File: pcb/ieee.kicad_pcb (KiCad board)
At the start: 2 copper layers, 152.4 x 114.3 mm, 45 parts, among them J1 Conn_01x20_Pin, J2 Conn_01x20_Pin, J3 Screw_Terminal_01x02, J4 I2C_LCD, J5 Conn_01x20_Pin, J6 Conn_01x20_Pin, M1 FL, M2 FR, M3 RL, M4 RR, M5 Corkscrew, M6 Crank, M7 Fingers, SW1 SW_SPST, U1 TB9051FTG, U10 TCS34725, U11 TCS34725, U12 TB9051FTG, U13 TB9051FTG, U14 IR_Transmitter, U2 TB9051FTG, U3 TB9051FTG, U4 TB9051FTG, U5 PCA9543AD_118, U6 SN74LVC8T245NSR, U7 DRV8833, U8 DRV8833, U9 D36V50F5

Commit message: Fix ERC issues and layout connectors
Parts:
- added R2: 100K, Resistor_THT:R_Axial_DIN0309_L9.0mm_D3.2mm_P15.24mm_Horizontal, F.Cu at (101.9, 119.7)
- added R4: 100K, Resistor_THT:R_Axial_DIN0309_L9.0mm_D3.2mm_P15.24mm_Horizontal, F.Cu at (101.9, 124.5)
- moved M6 314.1 mm to (160.3, 144.8), turned to -90 degrees
- moved U2 305.5 mm to (99.1, 110.7)
- moved J4 303.7 mm to (112.8, 113.8), turned to 180 degrees
- moved A2 302.5 mm to (114.0, 136.9), turned to -90 degrees
- moved U4 260.5 mm to (85.1, 116.1)
- moved S1 256.8 mm to (84.1, 144.8), turned to 90 degrees
- moved U13 250.4 mm to (153.9, 128.5), turned to -90 degrees
- moved JP1 250.4 mm to (199.9, 63.2)
- moved JP2 250.4 mm to (199.4, 58.2)
- moved JP3 250.4 mm to (178.5, 58.7)
- moved JP4 250.4 mm to (178.5, 62.3)
- moved U12 249.9 mm to (144.5, 66.0), turned to 0 degrees
- moved M7 249.5 mm to (147.1, 112.3), turned to 90 degrees
- moved U14 245.7 mm to (153.4, 96.0)
- moved R1 244.6 mm to (158.8, 42.9), turned to -90 degrees
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- renumbered A3 to A2, A2 to A3, J3 to J1, J1 to J2, J2 to J3, M3 to M2, M2 to M3, M7 to M5, M5 to M6, M6 to M7, R2 to R1, R1 to R3, U11 to U1, U4 to U10, U7 to U11, U8 to U12, U12 to U13, U13 to U14, U5 to U2, U9 to U3, U10 to U4, U14 to U5, U1 to U7, U3 to U8, U2 to U9
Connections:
- A1 pad 10: /pico_subsystem/RPI_RX -> /RPI_RX
- A1 pad 8: /pico_subsystem/RPI_TX -> /RPI_TX
- A3 pad 1: /pico_subsystem/RPI_RX -> /RPI_RX
- A3 pad 2: /pico_subsystem/RPI_TX -> /RPI_TX
- J2 pad 2: /SDA -> /RPI_SDA
- J2 pad 3: /SCL -> /RPI_SCL
- J5 pad 1: /pico_subsystem/RPI_RX -> /RPI_RX
- J5 pad 2: /pico_subsystem/RPI_TX -> /RPI_TX
- J6 pad 13: GND -> /pico_subsystem/PICO_AGND
- U12 pad 11: unconnected-(U8-IN3-Pad11) -> /RPI_GPIO10
- U12 pad 12: unconnected-(U8-IN4-Pad12) -> /RPI_GPIO11
- U12 pad 7: unconnected-(U8-IN1-Pad7) -> /RPI_GPIO8
- U12 pad 8: unconnected-(U8-IN2-Pad8) -> /RPI_GPIO9
- U13 pad 7: unconnected-(U12-PWM2-Pad7) -> /RPI_GPIO17
- U13 pad 8: unconnected-(U12-PWM1-Pad8) -> /RPI_GPIO16
- U14 pad 7: unconnected-(U13-PWM2-Pad7) -> /manipulation/CRANK_PWM2
- U14 pad 8: unconnected-(U13-PWM1-Pad8) -> /manipulation/CRANK_PWM1
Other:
- copper layers 2 -> 4

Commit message: Start routing
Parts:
- moved U6 33.2 mm to (175.3, 120.4), turned to 180 degrees
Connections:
- J6 pad 13: /pico_subsystem/PICO_AGND -> GND
- J6 pad 8: GND -> /pico_subsystem/PICO_AGND
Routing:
- net /pico_subsystem/FR_ENCB_5V: track 0.00 -> 139.0 mm
- net /pico_subsystem/FR_ENCA_5V: track 0.00 -> 137.3 mm
- net /pico_subsystem/RR_ENCA_5V: track 0.00 -> 132.4 mm
- net /pico_subsystem/RR_ENCB_5V: track 0.00 -> 130.5 mm
- net /pico_subsystem/FL_ENCB_5V: track 0.00 -> 121.6 mm
- net /pico_subsystem/FL_ENCA_5V: track 0.00 -> 121.1 mm
- net GND: track 0.00 -> 110.7 mm
- net /RPI_PWM3: track 0.00 -> 46.4 mm
- net ENABLE: track 0.00 -> 44.1 mm
- net /pico_subsystem/PICO_3V3: track 0.00 -> 43.1 mm
- net /pico_subsystem/FL_ENCA: track 0.00 -> 37.0 mm
- net /RPI_PWM2: track 0.00 -> 35.6 mm
- net /RPI_GPIO26: track 0.00 -> 31.6 mm
- net /pico_subsystem/FL_ENCB: track 0.00 -> 31.4 mm
- net /pico_subsystem/FR_ENCA: track 0.00 -> 28.3 mm
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
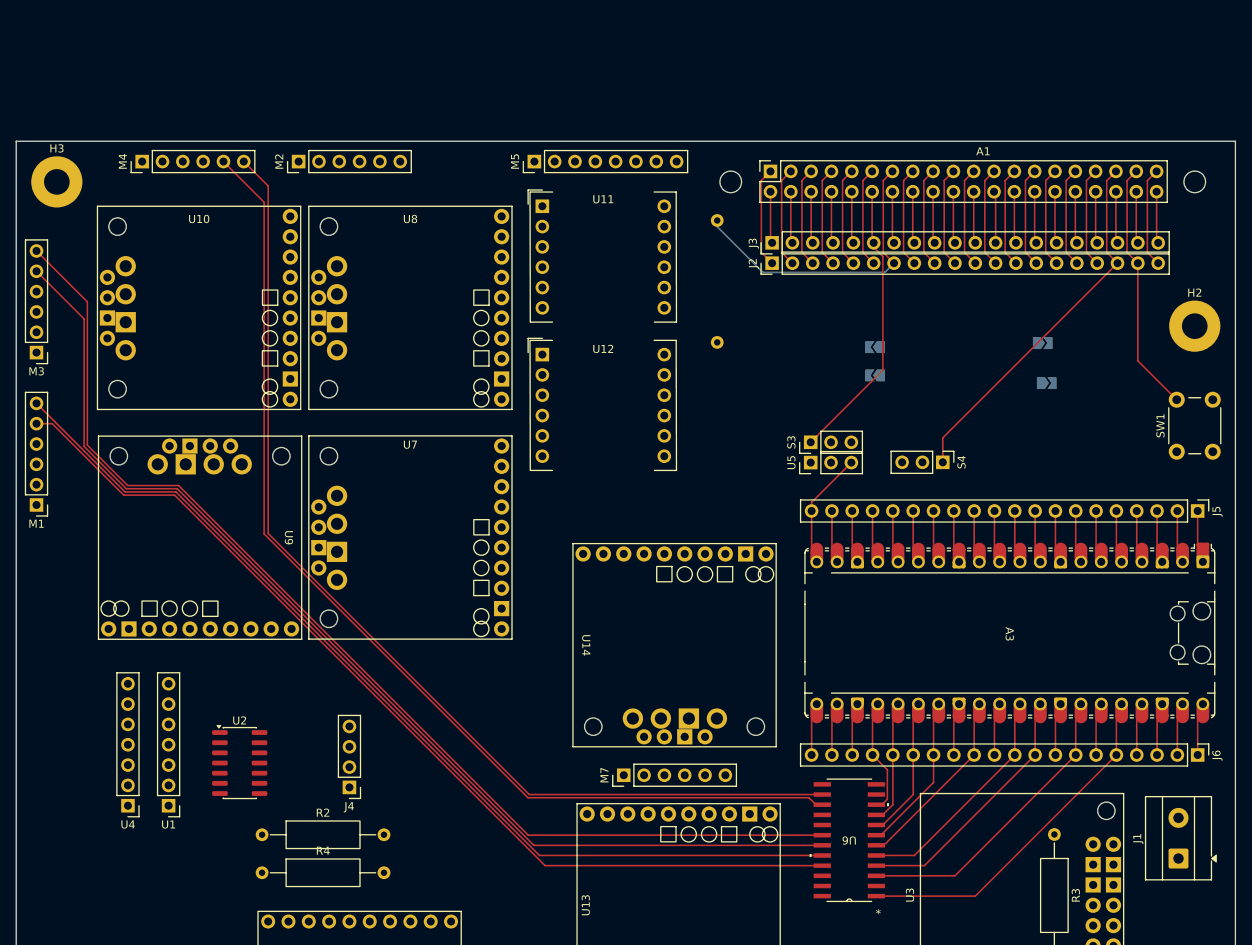
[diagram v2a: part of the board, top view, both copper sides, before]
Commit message: Route RPI and Pico breakouts
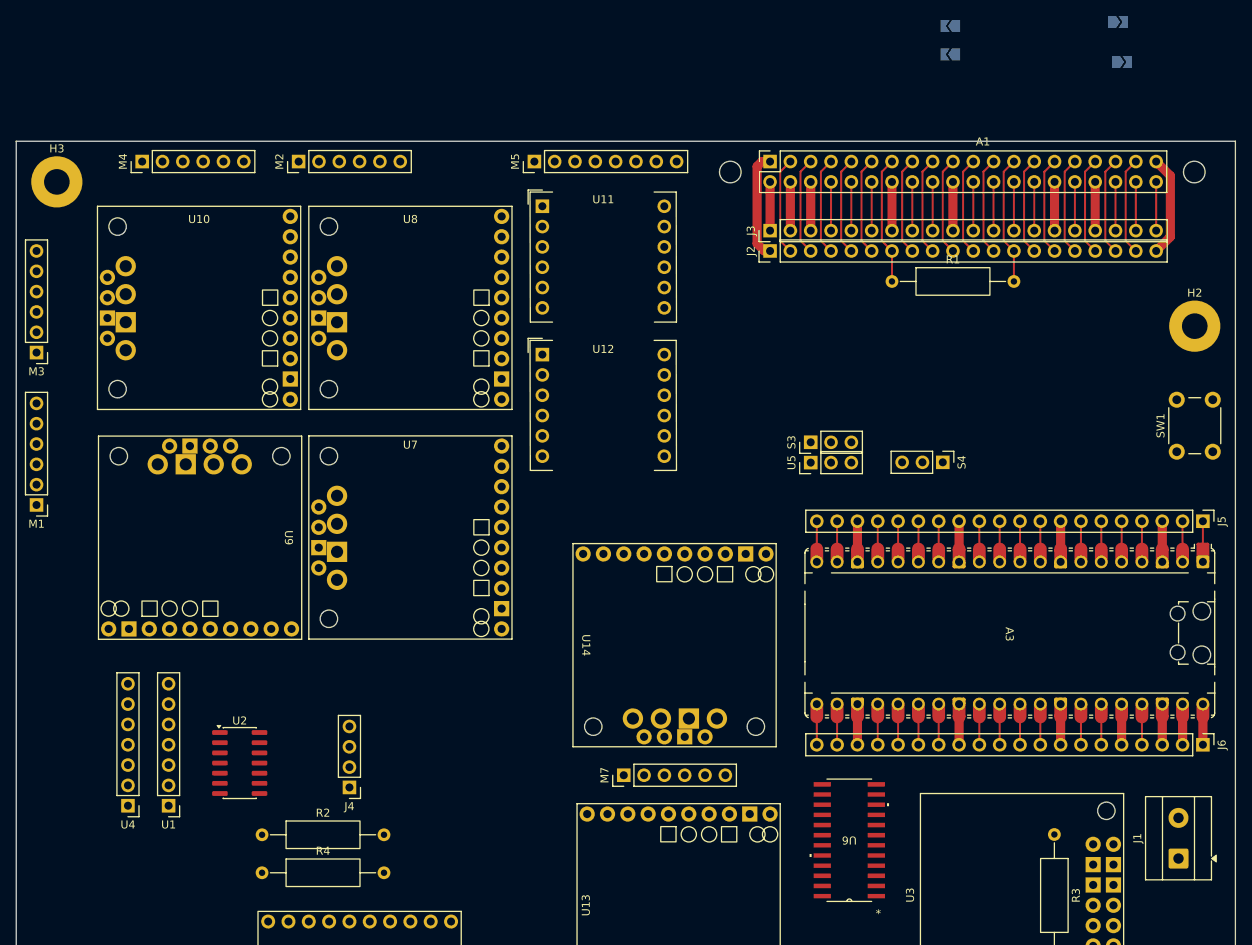
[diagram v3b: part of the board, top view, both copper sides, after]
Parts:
- R1: moved to F.Cu
- moved JP1 41.2 mm to (209.3, 23.1)
- moved JP2 41.2 mm to (208.8, 18.1)
- moved JP3 41.2 mm to (187.9, 18.6)
- moved JP4 41.2 mm to (187.9, 22.2)
- moved R1 23.1 mm to (180.6, 50.5), turned to 0 degrees
- moved J2 1.55 mm to (165.4, 46.7)
- moved J3 1.55 mm to (165.4, 44.2)
- moved J5 1.44 mm to (219.5, 80.5)
- moved J6 1.44 mm to (219.5, 108.5)
- moved A1 1.23 mm to (199.4, 12.4)
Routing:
- net /pico_subsystem/FR_ENCB_5V: track 139.0 -> 0.00 mm
- net /pico_subsystem/FR_ENCA_5V: track 137.3 -> 0.00 mm
- net /pico_subsystem/RR_ENCA_5V: track 132.4 -> 0.00 mm
- net /pico_subsystem/RR_ENCB_5V: track 130.5 -> 0.00 mm
- net /pico_subsystem/FL_ENCB_5V: track 121.6 -> 0.00 mm
- net /pico_subsystem/FL_ENCA_5V: track 121.1 -> 0.00 mm
- net /pico_subsystem/PICO_3V3: track 43.1 -> 5.08 mm
- net /RPI_PWM3: track 46.4 -> 12.2 mm
- net /pico_subsystem/FL_ENCA: track 37.0 -> 4.28 mm
- net /RPI_PWM2: track 35.6 -> 6.10 mm
- net /pico_subsystem/FL_ENCB: track 31.4 -> 4.28 mm
- net /pico_subsystem/FR_ENCA: track 28.3 -> 4.28 mm
- net ENABLE: track 44.1 -> 20.3 mm
- net /RPI_GPIO26: track 31.6 -> 12.2 mm
- net /pico_subsystem/FR_ENCB: track 22.7 -> 4.28 mm
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
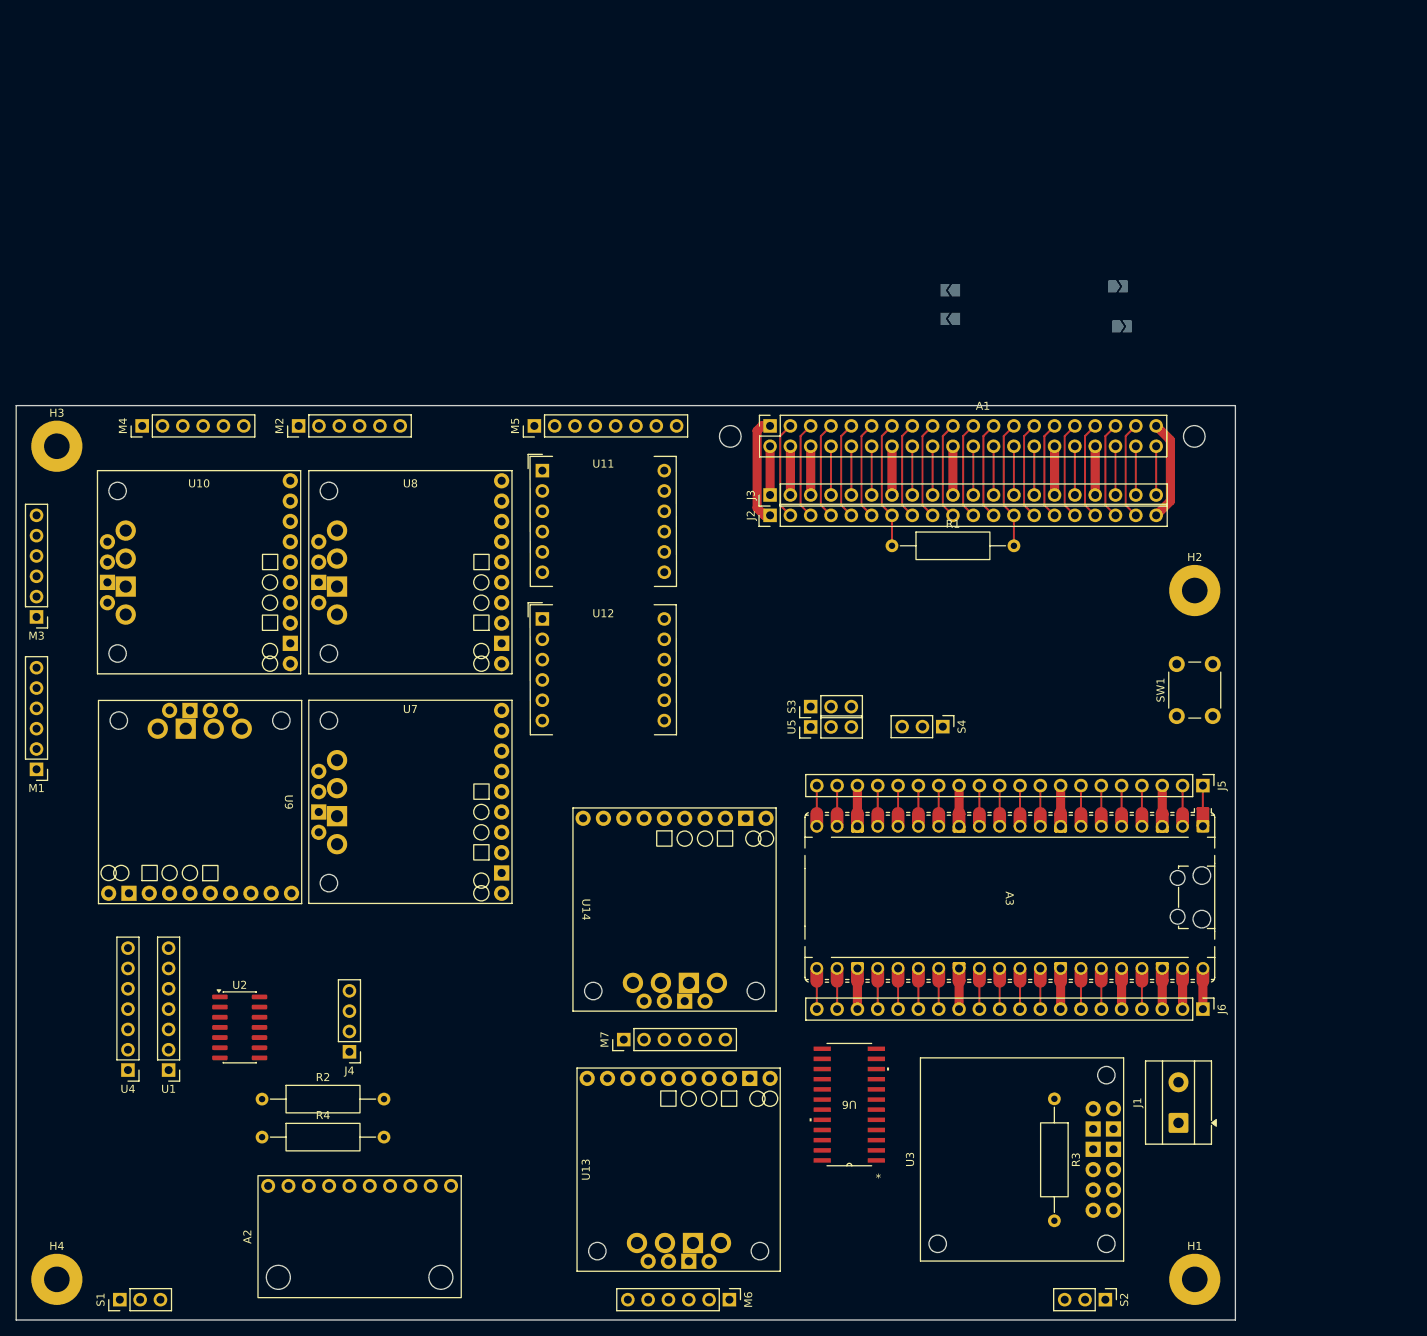
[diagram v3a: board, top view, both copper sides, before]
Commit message: Route I2C and planes
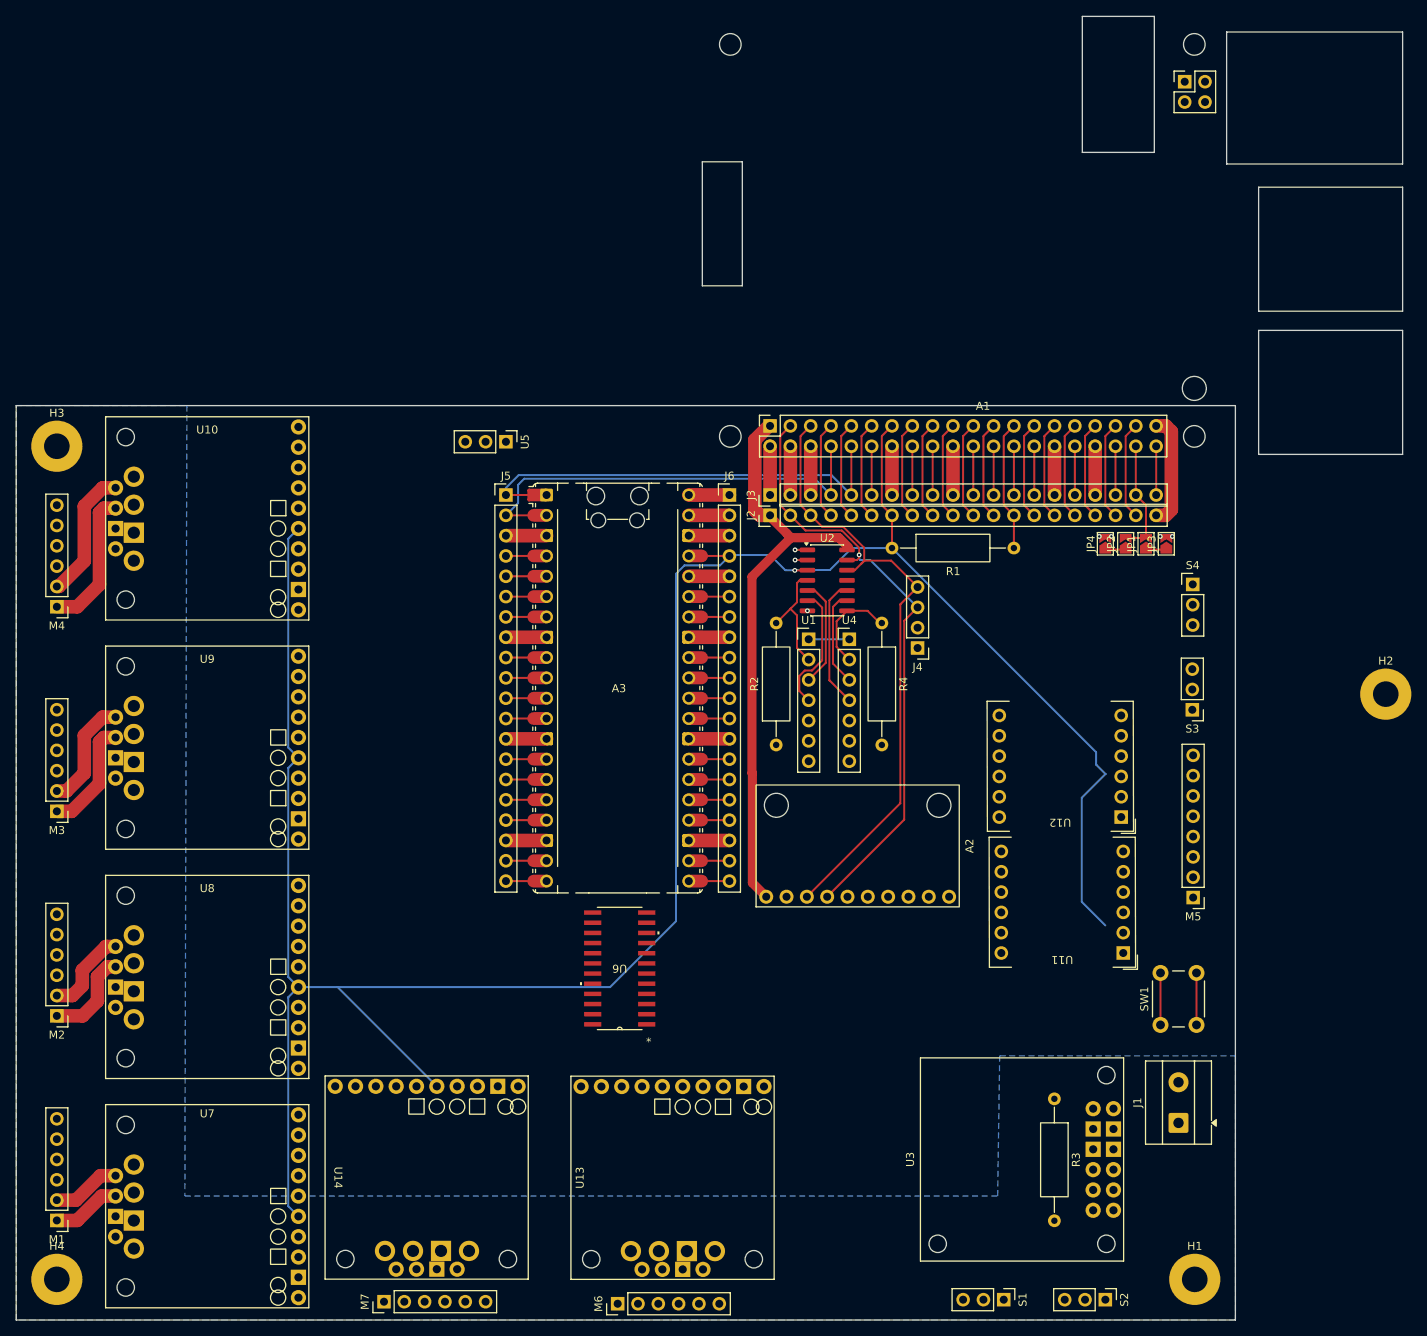
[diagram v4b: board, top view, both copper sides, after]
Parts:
- JP1, JP2, JP3, JP4: moved to F.Cu
- moved S1 110.5 mm to (194.6, 144.8), turned to -90 degrees
- moved U4 105.0 mm to (175.3, 62.2), turned to 0 degrees
- moved M5 101.3 mm to (218.2, 94.5), turned to 180 degrees
- moved R4 100.7 mm to (179.3, 60.2), turned to -90 degrees
- moved U1 96.4 mm to (170.2, 62.2), turned to 0 degrees
- moved J5 94.4 mm to (132.3, 44.2), turned to 0 degrees
- moved U2 92.3 mm to (172.5, 54.9)
- moved J6 87.4 mm to (160.3, 44.2), turned to 0 degrees
- moved J4 87.1 mm to (183.8, 63.3)
- moved M2 79.7 mm to (76.2, 109.3), turned to 180 degrees
- moved A2 79.1 mm to (176.3, 88.1), turned to 90 degrees
- moved R2 78.0 mm to (166.1, 75.4), turned to 90 degrees
- moved U11 74.5 mm to (201.9, 95.1), turned to 180 degrees
- moved U12 58.4 mm to (201.6, 78.1), turned to 180 degrees
- moved U8 56.6 mm to (95.0, 104.4)
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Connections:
- R2 pad 1: +3V3 -> +5V
- R4 pad 2: +3V3 -> +5V
- U1 pad 7: +3V3 -> +5V
- U13 pad 11: /manipulation/CORKSCREW_OUT2 -> /manipulation/CORKSCREW_OUT1
- U13 pad 12: /manipulation/CORKSCREW_OUT1 -> /manipulation/CORKSCREW_OUT2
- U4 pad 7: +3V3 -> +5V
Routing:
- net ENABLE: track 20.3 -> 313.3 mm, vias 0 -> 1
- net /RPI_SCL: track 12.2 -> 77.9 mm
- net /RPI_SDA: track 12.2 -> 76.5 mm, vias 0 -> 1
- net +3V3: track 25.8 -> 85.1 mm
- net /RPI_RX: track 11.2 -> 56.9 mm
- net /RPI_TX: track 11.2 -> 55.9 mm
- net /pico_subsystem/RR_OUT2: track 0.00 -> 17.7 mm
- net /pico_subsystem/RR_OUT1: track 0.00 -> 16.5 mm
- net Net-(U2-SC1): track 0.00 -> 16.2 mm
- net Net-(U1-SCL): track 0.00 -> 16.0 mm
- net Net-(U1-INT): track 0.00 -> 14.8 mm
- net /pico_subsystem/FR_OUT2: track 0.00 -> 14.2 mm
- net /pico_subsystem/FR_OUT1: track 0.00 -> 13.9 mm
- net Net-(U1-SDA): track 0.00 -> 13.6 mm
- net Net-(U2-*INT1): track 0.00 -> 12.3 mm
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- added copper zone on In2.Cu, net +5V
- added copper zone on B.Cu, net +BATT
- added copper zone on In1.Cu, net GND
